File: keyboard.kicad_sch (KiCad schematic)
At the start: 73 parts, among them SW1 SW_SPDT, U1 nice_nano

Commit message: Cut corner version
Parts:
- added H8: Mnt, TestPoint:TestPoint_THTPad_D4.0mm_Drill2.0mm, symbol Mechanical:MountingHole_Pad
- U1: symbol NiceNano:nice_nano -> NiceNano:nice_nano_nocenter
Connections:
- net GND: now also H1.1, H8.1; no longer SW1.2 (B)
- net col5: now also U1.15 (P1.11)
- net col6: now also U1.14 (NFC2/P0.10); no longer U1.15 (P1.11)
- net col9: now also U1.7 (P0.22)
- net at SW1.1 (A): no longer H1.1
- net BATIN: now reaches SW1.3 (C)
- net BATIN: now also H2.1, SW1.2 (B), U1.24 (BATIN/P0.04)
- no-connect marks 9 -> 5
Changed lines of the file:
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@@
   (junction (at 121.92 49.53) (diameter 0) (color 0 0 0 0)
   )
-  (no_connect (at 33.02 160.02))
+  (no_connect (at 33.02 147.32))
+  (no_connect (at 33.02 144.78))
   (no_connect (at 33.02 162.56))
   (no_connect (at 68.58 149.86))
   (no_connect (at 68.58 152.4))
-  (no_connect (at 50.8 185.42))
-  (no_connect (at 46.99 185.42))
-  (no_connect (at 43.18 185.42))
-  (no_connect (at 68.58 170.18))
-  (no_connect (at 68.58 172.72))
   (wire (pts (xy 186.69 60.96) (xy 212.09 60.96))
     (stroke (width 0) (type default) (color 0 0 0 0))
@@
     (stroke (width 0) (type default) (color 0 0 0 0))
   )
+  (wire (pts (xy 88.9 148.59) (xy 78.74 148.59))
+    (stroke (width 0) (type default) (color 0 0 0 0))
+  )
   (wire (pts (xy 161.29 35.56) (xy 186.69 35.56))
     (stroke (width 0) (type default) (color 0 0 0 0))
@@
     (stroke (width 0) (type default) (color 0 0 0 0))
   )
-  (wire (pts (xy 77.47 161.29) (xy 77.47 144.78))
-    (stroke (width 0) (type default) (color 0 0 0 0))
-  )
   (wire (pts (xy 161.29 80.01) (xy 161.29 81.28))
     (stroke (width 0) (type default) (color 0 0 0 0))
@@
     (stroke (width 0) (type default) (color 0 0 0 0))
   )
-  (wire (pts (xy 115.57 148.59) (xy 99.06 148.59))
-    (stroke (width 0) (type default) (color 0 0 0 0))
-  )
   (wire (pts (xy 115.57 49.53) (xy 121.92 49.53))
     (stroke (width 0) (type default) (color 0 0 0 0))
@@
     (stroke (width 0) (type default) (color 0 0 0 0))
   )
-  (wire (pts (xy 77.47 144.78) (xy 68.58 144.78))
-    (stroke (width 0) (type default) (color 0 0 0 0))
-  )
   (wire (pts (xy 172.72 16.51) (xy 172.72 24.13))
     (stroke (width 0) (type default) (color 0 0 0 0))
@@
     (stroke (width 0) (type default) (color 0 0 0 0))
   )
+  (wire (pts (xy 78.74 144.78) (xy 68.58 144.78))
+    (stroke (width 0) (type default) (color 0 0 0 0))
+  )
   (wire (pts (xy 135.89 54.61) (xy 135.89 55.88))
     (stroke (width 0) (type default) (color 0 0 0 0))
@@
     (stroke (width 0) (type default) (color 0 0 0 0))
   )
+  (wire (pts (xy 115.57 161.29) (xy 99.06 161.29))
+    (stroke (width 0) (type default) (color 0 0 0 0))
+  )
   (wire (pts (xy 147.32 74.93) (xy 147.32 49.53))
     (stroke (width 0) (type default) (color 0 0 0 0))
@@
     (stroke (width 0) (type default) (color 0 0 0 0))
   )
+  (wire (pts (xy 78.74 148.59) (xy 78.74 144.78))
+    (stroke (width 0) (type default) (color 0 0 0 0))
+  )
   (wire (pts (xy 217.17 74.93) (xy 223.52 74.93))
     (stroke (width 0) (type default) (color 0 0 0 0))
@@
     (stroke (width 0) (type default) (color 0 0 0 0))
   )
+  (wire (pts (xy 99.06 161.29) (xy 99.06 151.13))
+    (stroke (width 0) (type default) (color 0 0 0 0))
+  )
   (wire (pts (xy 223.52 100.33) (xy 223.52 74.93))
     (stroke (width 0) (type default) (color 0 0 0 0))
   )
-  (wire (pts (xy 115.57 161.29) (xy 77.47 161.29))
-    (stroke (width 0) (type default) (color 0 0 0 0))
-  )
   (wire (pts (xy 34.29 60.96) (xy 59.69 60.96))
     (stroke (width 0) (type default) (color 0 0 0 0))
@@
   )
   (wire (pts (xy 85.09 35.56) (xy 110.49 35.56))
-    (stroke (width 0) (type default) (color 0 0 0 0))
-  )
-  (wire (pts (xy 99.06 148.59) (xy 99.06 146.05))
     (stroke (width 0) (type default) (color 0 0 0 0))
   )
@@
     (effects (font (size 1.27 1.27)) (justify right bottom))
   )
+  (label "BATIN" (at 68.58 144.78 0)
+    (effects (font (size 1.27 1.27)) (justify left bottom))
+  )
+  (label "GND" (at 129.54 177.8 270)
+    (effects (font (size 1.27 1.27)) (justify right bottom))
+  )
   (label "GND" (at 99.06 177.8 270)
     (effects (font (size 1.27 1.27)) (justify right bottom))
@@
     (effects (font (size 1.27 1.27)) (justify right bottom))
   )
+  (label "BATIN" (at 115.57 161.29 0)
+    (effects (font (size 1.27 1.27)) (justify left bottom))
+  )
   (label "GND" (at 33.02 152.4 180)
     (effects (font (size 1.27 1.27)) (justify right bottom))
   )
+  (label "col9" (at 33.02 160.02 180)
+    (effects (font (size 1.27 1.27)) (justify right bottom))
+  )
+  (label "col6" (at 68.58 170.18 0)
+    (effects (font (size 1.27 1.27)) (justify left bottom))
+  )
+  (label "GND" (at 115.57 148.59 0)
+    (effects (font (size 1.27 1.27)) (justify left bottom))
+  )
   (label "col4" (at 68.58 165.1 0)
     (effects (font (size 1.27 1.27)) (justify left bottom))
@@
     (effects (font (size 1.27 1.27)) (justify right bottom))
   )
-  (label "col6" (at 68.58 167.64 0)
+  (label "col5" (at 68.58 167.64 0)
     (effects (font (size 1.27 1.27)) (justify left bottom))
   )
@@
     (effects (font (size 1.27 1.27)) (justify left bottom))
   )
-  (label "GND" (at 88.9 148.59 180)
+  (label "BATIN" (at 88.9 148.59 180)
     (effects (font (size 1.27 1.27)) (justify right bottom))
   )
@@
     (pin "2")
   )
-  (symbol (lib_id "NiceNano:nice_nano") (at 50.8 158.75 0) (unit 1)
+  (symbol (lib_id "NiceNano:nice_nano_nocenter") (at 50.8 158.75 0) (unit 1)
     (in_bom yes) (on_board yes) (fields_autoplaced)
     (property "Reference" "U1" (id 0) (at 50.8 134.62 0)
@@
     (pin "24")
     (pin "3")
-    (pin "31")
-    (pin "32")
-    (pin "33")
     (pin "4")
     (pin "5")
@@
     (pin "2")
   )
+  (symbol (lib_id "Mechanical:MountingHole_Pad") (at 129.54 175.26 0) (unit 1)
+    (in_bom yes) (on_board yes) (fields_autoplaced)
+    (property "Reference" "H8" (id 0) (at 132.08 172.7199 0)
+      (effects (font (size 1.27 1.27)) (justify left))
+    )
+    (property "Value" "Mnt" (id 1) (at 132.08 175.2599 0)
+      (effects (font (size 1.27 1.27)) (justify left))
+    )
+    (property "Footprint" "TestPoint:TestPoint_THTPad_D4.0mm_Drill2.0mm" (id 2) (at 129.54 175.26 0)
+      (effects (font (size 1.27 1.27)) hide)
+    )
+    (property "Datasheet" "~" (id 3) (at 129.54 175.26 0)
+      (effects (font (size 1.27 1.27)) hide)
+    )
+    (pin "1")
+  )
   (symbol (lib_id "MX_Alps_Hybrid:MX-NoLED") (at 86.36 50.8 0) (unit 1)
     (in_bom yes) (on_board yes)
@@
       (reference "H7") (unit 1) (value "Mnt") (footprint "TestPoint:TestPoint_THTPad_D4.0mm_Drill2.0mm")
     )
+    (path "/6e5b64a0-e007-4872-81d5-b9c48adbb71a"
+      (reference "H8") (unit 1) (value "Mnt") (footprint "TestPoint:TestPoint_THTPad_D4.0mm_Drill2.0mm")
+    )
     (path "/e6521bef-4109-48f7-8b88-4121b0468927"

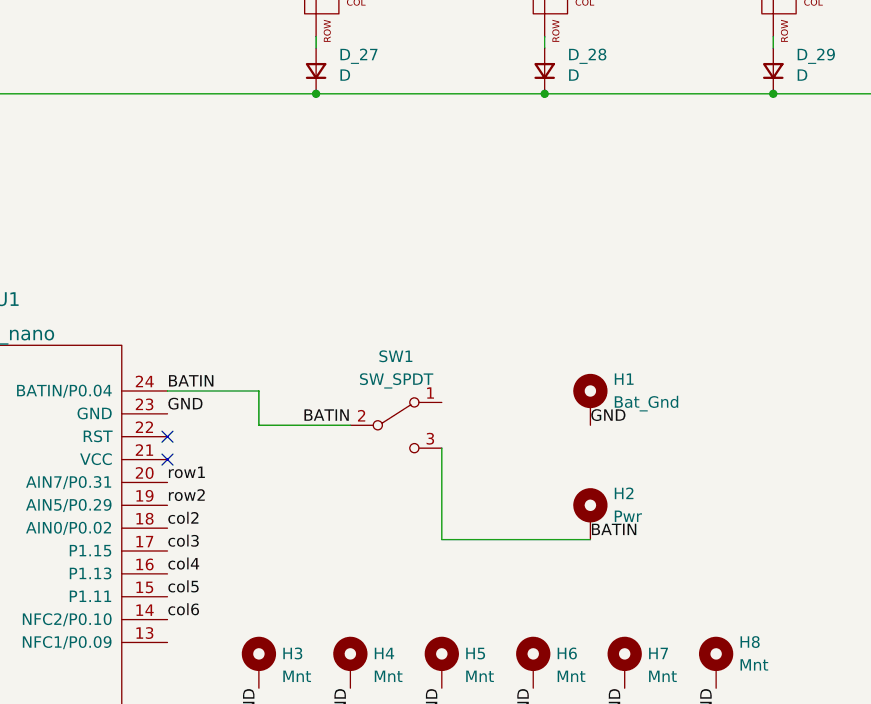
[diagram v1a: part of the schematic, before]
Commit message: Add reset pins
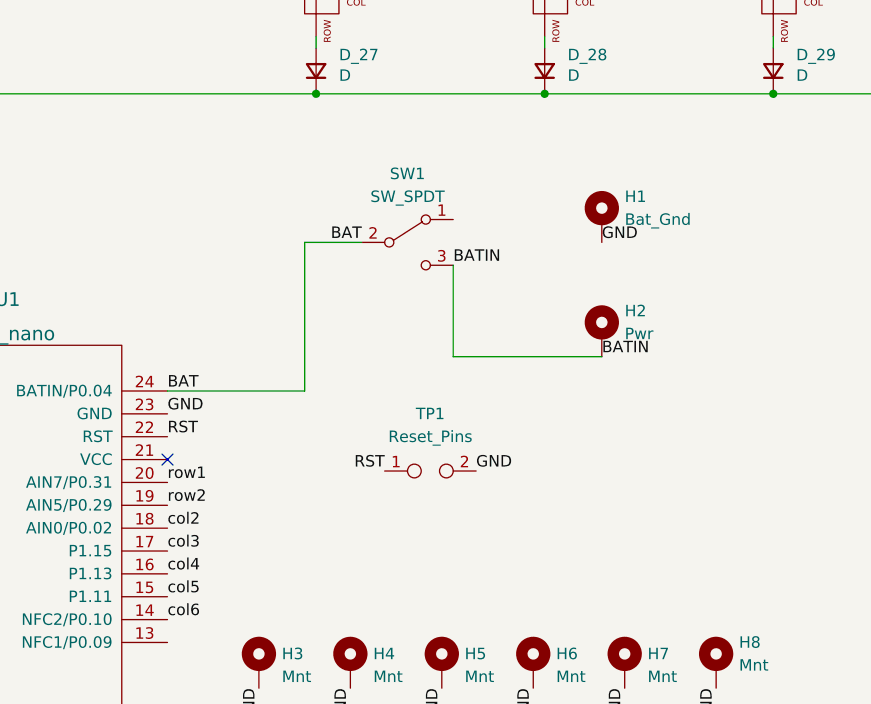
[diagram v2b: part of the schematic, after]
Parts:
- added TP1: Reset_Pins, ProjectLocal:ResetSW, symbol Connector:TestPoint_2Pole
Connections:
- net BATIN: no longer SW1.2 (B), U1.24 (BATIN/P0.04)
- net GND: now also TP1.2
- net RST: now reaches U1.22 (RST)
- net RST: now also TP1.1
- new net BAT: SW1.2 (B), U1.24 (BATIN/P0.04)
- no-connect marks 5 -> 4
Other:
- moved on the sheet: H1, H2, SW1
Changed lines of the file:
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@@
   (no_connect (at 33.02 144.78))
   (no_connect (at 33.02 162.56))
-  (no_connect (at 68.58 149.86))
   (no_connect (at 68.58 152.4))
   (wire (pts (xy 186.69 60.96) (xy 212.09 60.96))
@@
     (stroke (width 0) (type default) (color 0 0 0 0))
   )
+  (wire (pts (xy 83.82 128.27) (xy 83.82 144.78))
+    (stroke (width 0) (type default) (color 0 0 0 0))
+  )
   (wire (pts (xy 59.69 60.96) (xy 85.09 60.96))
     (stroke (width 0) (type default) (color 0 0 0 0))
@@
     (stroke (width 0) (type default) (color 0 0 0 0))
   )
-  (wire (pts (xy 88.9 148.59) (xy 78.74 148.59))
-    (stroke (width 0) (type default) (color 0 0 0 0))
-  )
   (wire (pts (xy 161.29 35.56) (xy 186.69 35.56))
     (stroke (width 0) (type default) (color 0 0 0 0))
@@
     (stroke (width 0) (type default) (color 0 0 0 0))
   )
-  (wire (pts (xy 78.74 144.78) (xy 68.58 144.78))
+  (wire (pts (xy 68.58 144.78) (xy 83.82 144.78))
     (stroke (width 0) (type default) (color 0 0 0 0))
   )
@@
     (stroke (width 0) (type default) (color 0 0 0 0))
   )
+  (wire (pts (xy 90.17 128.27) (xy 83.82 128.27))
+    (stroke (width 0) (type default) (color 0 0 0 0))
+  )
   (wire (pts (xy 90.17 24.13) (xy 96.52 24.13))
     (stroke (width 0) (type default) (color 0 0 0 0))
@@
     (stroke (width 0) (type default) (color 0 0 0 0))
   )
-  (wire (pts (xy 115.57 161.29) (xy 99.06 161.29))
+  (wire (pts (xy 116.84 140.97) (xy 100.33 140.97))
     (stroke (width 0) (type default) (color 0 0 0 0))
   )
@@
     (stroke (width 0) (type default) (color 0 0 0 0))
   )
-  (wire (pts (xy 78.74 148.59) (xy 78.74 144.78))
-    (stroke (width 0) (type default) (color 0 0 0 0))
-  )
   (wire (pts (xy 217.17 74.93) (xy 223.52 74.93))
     (stroke (width 0) (type default) (color 0 0 0 0))
@@
     (stroke (width 0) (type default) (color 0 0 0 0))
   )
-  (wire (pts (xy 99.06 161.29) (xy 99.06 151.13))
+  (wire (pts (xy 100.33 140.97) (xy 100.33 130.81))
     (stroke (width 0) (type default) (color 0 0 0 0))
   )
@@
     (effects (font (size 1.27 1.27)) (justify right bottom))
   )
+  (label "BATIN" (at 100.33 130.81 0)
+    (effects (font (size 1.27 1.27)) (justify left bottom))
+  )
   (label "col1" (at 33.02 157.48 180)
     (effects (font (size 1.27 1.27)) (justify right bottom))
@@
     (effects (font (size 1.27 1.27)) (justify right bottom))
   )
+  (label "GND" (at 102.87 153.67 0)
+    (effects (font (size 1.27 1.27)) (justify left bottom))
+  )
   (label "col0" (at 33.02 154.94 180)
     (effects (font (size 1.27 1.27)) (justify right bottom))
   )
-  (label "BATIN" (at 68.58 144.78 0)
+  (label "BAT" (at 68.58 144.78 0)
     (effects (font (size 1.27 1.27)) (justify left bottom))
   )
@@
     (effects (font (size 1.27 1.27)) (justify right bottom))
   )
-  (label "BATIN" (at 115.57 161.29 0)
+  (label "BATIN" (at 116.84 140.97 0)
+    (effects (font (size 1.27 1.27)) (justify left bottom))
+  )
+  (label "RST" (at 68.58 149.86 0)
     (effects (font (size 1.27 1.27)) (justify left bottom))
   )
@@
     (effects (font (size 1.27 1.27)) (justify left bottom))
   )
-  (label "GND" (at 115.57 148.59 0)
+  (label "GND" (at 116.84 128.27 0)
     (effects (font (size 1.27 1.27)) (justify left bottom))
   )
@@
     (effects (font (size 1.27 1.27)) (justify left bottom))
   )
+  (label "RST" (at 92.71 153.67 180)
+    (effects (font (size 1.27 1.27)) (justify right bottom))
+  )
   (label "col8" (at 33.02 170.18 180)
     (effects (font (size 1.27 1.27)) (justify right bottom))
@@
     (effects (font (size 1.27 1.27)) (justify left bottom))
   )
-  (label "BATIN" (at 88.9 148.59 180)
+  (label "BAT" (at 90.17 128.27 180)
     (effects (font (size 1.27 1.27)) (justify right bottom))
   )
@@
     (pin "2")
   )
-  (symbol (lib_id "Switch:SW_SPDT") (at 93.98 148.59 0) (unit 1)
+  (symbol (lib_id "Switch:SW_SPDT") (at 95.25 128.27 0) (unit 1)
     (in_bom yes) (on_board yes) (fields_autoplaced)
-    (property "Reference" "SW1" (id 0) (at 93.98 140.97 0))
-    (property "Value" "SW_SPDT" (id 1) (at 93.98 143.51 0))
-    (property "Footprint" "Button_Switch_THT:SW_Slide_1P2T_CK_OS102011MS2Q" (id 2) (at 93.98 148.59 0)
-      (effects (font (size 1.27 1.27)) hide)
-    )
-    (property "Datasheet" "~" (id 3) (at 93.98 148.59 0)
+    (property "Reference" "SW1" (id 0) (at 95.25 120.65 0))
+    (property "Value" "SW_SPDT" (id 1) (at 95.25 123.19 0))
+    (property "Footprint" "Button_Switch_THT:SW_Slide_1P2T_CK_OS102011MS2Q" (id 2) (at 95.25 128.27 0)
+      (effects (font (size 1.27 1.27)) hide)
+    )
+    (property "Datasheet" "~" (id 3) (at 95.25 128.27 0)
       (effects (font (size 1.27 1.27)) hide)
     )
@@
     (property "Datasheet" "" (id 3) (at 187.96 50.8 0)
       (effects (font (size 1.524 1.524)))
+    )
+    (pin "1")
+    (pin "2")
+  )
+  (symbol (lib_id "Connector:TestPoint_2Pole") (at 97.79 153.67 0) (unit 1)
+    (in_bom yes) (on_board yes) (fields_autoplaced)
+    (property "Reference" "TP1" (id 0) (at 97.79 147.32 0))
+    (property "Value" "Reset_Pins" (id 1) (at 97.79 149.86 0))
+    (property "Footprint" "ProjectLocal:ResetSW" (id 2) (at 97.79 153.67 0)
+      (effects (font (size 1.27 1.27)) hide)
+    )
+    (property "Datasheet" "~" (id 3) (at 97.79 153.67 0)
+      (effects (font (size 1.27 1.27)) hide)
     )
     (pin "1")
@@
     (pin "2")
   )
-  (symbol (lib_id "Mechanical:MountingHole_Pad") (at 115.57 158.75 0) (unit 1)
+  (symbol (lib_id "Mechanical:MountingHole_Pad") (at 116.84 138.43 0) (unit 1)
     (in_bom yes) (on_board yes) (fields_autoplaced)
-    (property "Reference" "H2" (id 0) (at 118.11 156.2099 0)
+    (property "Reference" "H2" (id 0) (at 119.38 135.8899 0)
       (effects (font (size 1.27 1.27)) (justify left))
     )
-    (property "Value" "Pwr" (id 1) (at 118.11 158.7499 0)
+    (property "Value" "Pwr" (id 1) (at 119.38 138.4299 0)
       (effects (font (size 1.27 1.27)) (justify left))
     )
-    (property "Footprint" "TestPoint:TestPoint_THTPad_D2.0mm_Drill1.0mm" (id 2) (at 115.57 158.75 0)
+    (property "Footprint" "TestPoint:TestPoint_THTPad_D2.0mm_Drill1.0mm" (id 2) (at 116.84 138.43 0)
       (effects (font (size 1.27 1.27)) (justify right) hide)
     )
-    (property "Datasheet" "~" (id 3) (at 115.57 158.75 0)
+    (property "Datasheet" "~" (id 3) (at 116.84 138.43 0)
       (effects (font (size 1.27 1.27)) hide)
     )
@@
     (pin "2")
   )
-  (symbol (lib_id "Mechanical:MountingHole_Pad") (at 115.57 146.05 0) (unit 1)
+  (symbol (lib_id "Mechanical:MountingHole_Pad") (at 116.84 125.73 0) (unit 1)
     (in_bom yes) (on_board yes) (fields_autoplaced)
-    (property "Reference" "H1" (id 0) (at 118.11 143.5099 0)
+    (property "Reference" "H1" (id 0) (at 119.38 123.1899 0)
       (effects (font (size 1.27 1.27)) (justify left))
     )
-    (property "Value" "Bat_Gnd" (id 1) (at 118.11 146.0499 0)
+    (property "Value" "Bat_Gnd" (id 1) (at 119.38 125.7299 0)
       (effects (font (size 1.27 1.27)) (justify left))
     )
-    (property "Footprint" "TestPoint:TestPoint_THTPad_D2.0mm_Drill1.0mm" (id 2) (at 115.57 146.05 0)
-      (effects (font (size 1.27 1.27)) hide)
-    )
-    (property "Datasheet" "~" (id 3) (at 115.57 146.05 0)
+    (property "Footprint" "TestPoint:TestPoint_THTPad_D2.0mm_Drill1.0mm" (id 2) (at 116.84 125.73 0)
+      (effects (font (size 1.27 1.27)) hide)
+    )
+    (property "Datasheet" "~" (id 3) (at 116.84 125.73 0)
       (effects (font (size 1.27 1.27)) hide)
     )
@@
       (reference "SW1") (unit 1) (value "SW_SPDT") (footprint "Button_Switch_THT:SW_Slide_1P2T_CK_OS102011MS2Q")
     )
+    (path "/25f56646-782f-4b6e-b1fc-4da948f857db"
+      (reference "TP1") (unit 1) (value "Reset_Pins") (footprint "ProjectLocal:ResetSW")
+    )
     (path "/4a3136df-385b-416b-a9b3-d730d73e2ec4"
